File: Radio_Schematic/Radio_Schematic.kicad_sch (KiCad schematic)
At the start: 0 parts

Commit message: Updated Radio Schematic
Updated the schematic used for our radio, adding the Arduino nano
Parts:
- added A1: Arduino_Nano_v3.x, Module:Arduino_Nano, symbol MCU_Module:Arduino_Nano_v3.x
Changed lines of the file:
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@@
 	(generator_version "10.0")
 	(paper "A4")
+	(symbol
+		(lib_id "MCU_Module:Arduino_Nano_v3.x")
+		(at 95.25 85.09 0)
+		(unit 1)
+		(body_style 1)
+		(exclude_from_sim no)
+		(in_bom yes)
+		(on_board yes)
+		(in_pos_files yes)
+		(dnp no)
+		(fields_autoplaced yes)
+		(property "Reference" "A1"
+			(at 99.9333 110.49 0)
+			(show_name no)
+			(do_not_autoplace no)
+			(effects
+				(font
+					(size 1.27 1.27)
+				)
+				(justify left)
+			)
+		)
+		(property "Value" "Arduino_Nano_v3.x"
+			(at 99.9333 113.03 0)
+			(show_name no)
+			(do_not_autoplace no)
+			(effects
+				(font
+					(size 1.27 1.27)
+				)
+				(justify left)
+			)
+		)
+		(property "Footprint" "Module:Arduino_Nano"
+			(at 95.25 85.09 0)
+			(hide yes)
+			(show_name no)
+			(do_not_autoplace no)
+			(effects
+				(font
+					(size 1.27 1.27)
+					(italic yes)
+				)
+			)
+		)
+		(property "Datasheet" "http://www.mouser.com/pdfdocs/Gravitech_Arduino_Nano3_0.pdf"
+			(at 95.25 85.09 0)
+			(hide yes)
+			(show_name no)
+			(do_not_autoplace no)
+			(effects
+				(font
+					(size 1.27 1.27)
+				)
+			)
+		)
+		(property "Description" "Arduino Nano v3.x"
+			(at 95.25 85.09 0)
+			(hide yes)
+			(show_name no)
+			(do_not_autoplace no)
+			(effects
+				(font
+					(size 1.27 1.27)
+				)
+			)
+		)
+		(pin "9"
+		)
+		(pin "13"
+		)
+		(pin "4"
+		)
+		(pin "14"
+		)
+		(pin "1"
+		)
+		(pin "3"
+		)
+		(pin "11"
+		)
+		(pin "2"
+		)
+		(pin "5"
+		)
+		(pin "6"
+		)
+		(pin "7"
+		)
+		(pin "12"
+		)
+		(pin "8"
+		)
+		(pin "10"
+		)
+		(pin "19"
+		)
+		(pin "22"
+		)
+		(pin "17"
+		)
+		(pin "29"
+		)
+		(pin "30"
+		)
+		(pin "18"
+		)
+		(pin "16"
+		)
+		(pin "21"
+		)
+		(pin "23"
+		)
+		(pin "24"
+		)
+		(pin "15"
+		)
+		(pin "20"
+		)
+		(pin "25"
+		)
+		(pin "26"
+		)
+		(pin "27"
+		)
+		(pin "28"
+		)
+		(instances
+			(project "Radio_Schematic"
+				(path "/45b700f0-d372-44fb-92b6-26c156c2429c"
+					(reference "A1")
+					(unit 1)
+				)
+			)
+		)
+	)
 	(sheet_instances
 		(path "/"

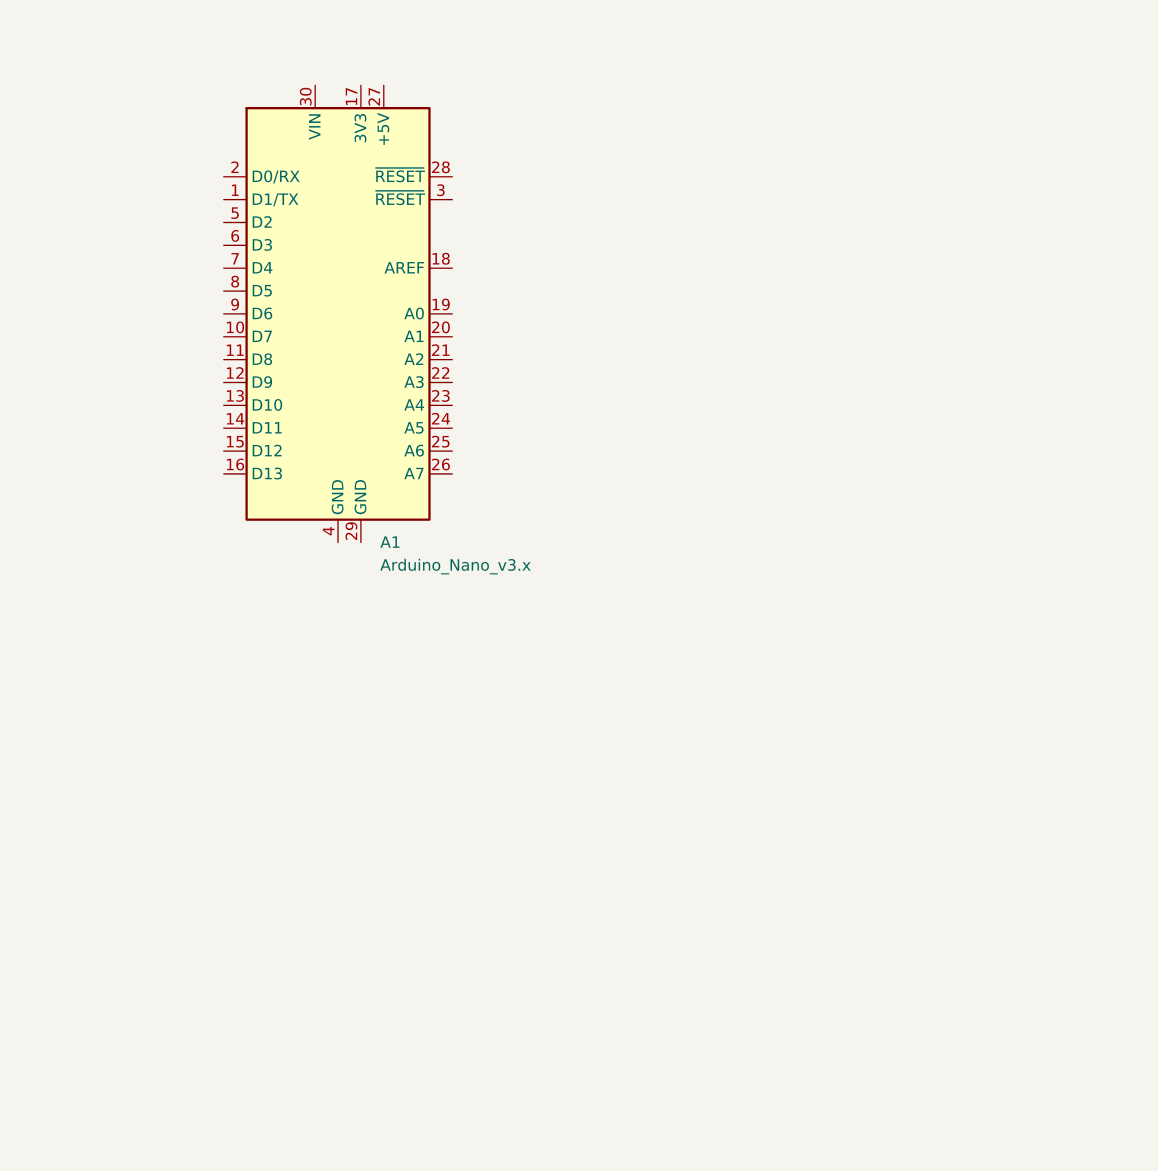
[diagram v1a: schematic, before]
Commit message: Schematic updates
Added more parts to radio schematic
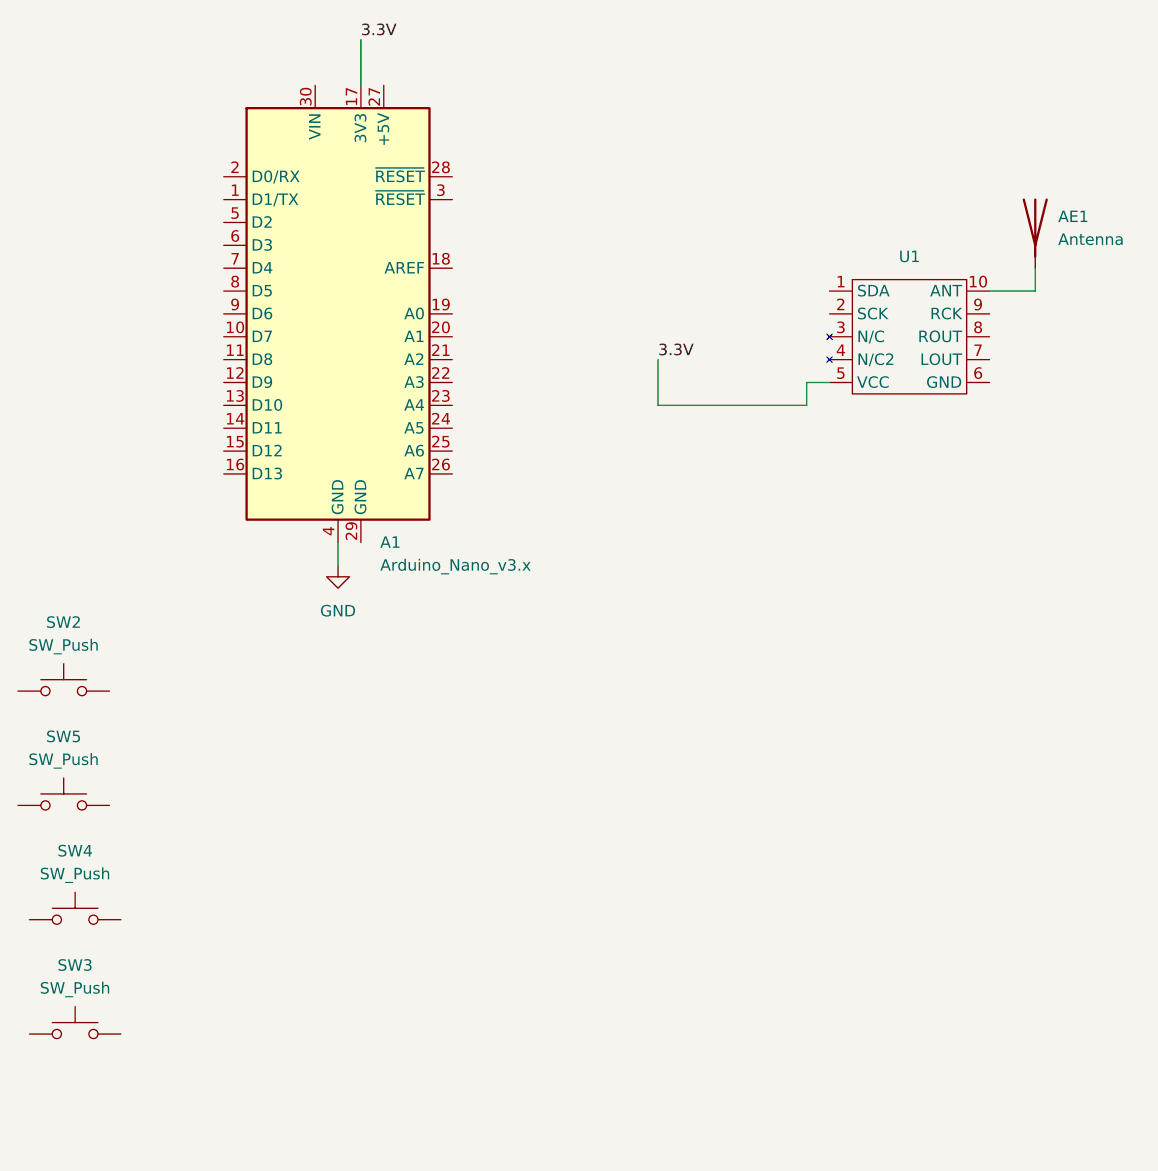
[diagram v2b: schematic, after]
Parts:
- added AE1: Antenna, symbol Device:Antenna
- added SW2, SW3, SW4, SW5: SW_Push, Package_DFN_QFN:Texas_RVA_VQFN-16-1EP_3.5x3.5mm_P0.5mm_EP2.14x2.14mm_ThermalVias, symbol Switch:SW_Push
- added U1: (no value), symbol New_Library:RDA5807M
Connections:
- net 3.3V: now reaches A1.17 (3V3)
- net 3.3V: now also U1.5 (VCC)
- net GND: now reaches A1.4 (GND)
- new net: AE1.1 (A), U1.10 (ANT)

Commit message: Updates
updated Git and radio schematic
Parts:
- removed SW2, SW5: SW_Push, Package_DFN_QFN:Texas_RVA_VQFN-16-1EP_3.5x3.5mm_P0.5mm_EP2.14x2.14mm_ThermalVias, symbol Switch:SW_Push
- added SW6: SW_Push, Package_DFN_QFN:Texas_RVA_VQFN-16-1EP_3.5x3.5mm_P0.5mm_EP2.14x2.14mm_ThermalVias, symbol Switch:SW_Push
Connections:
- net GND: now also A1.3 (~{RESET}), U1.6 (GND)
- net at U1.1 (SDA): now also A1.23 (A4)
- net at U1.2 (SCK): now also A1.24 (A5)
- net at SW4.2: now also A1.14 (D11)
- net at SW3.2: now also A1.15 (D12)
- net at A1.16 (D13): now also SW6.2
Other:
- moved on the sheet: SW3, SW4
